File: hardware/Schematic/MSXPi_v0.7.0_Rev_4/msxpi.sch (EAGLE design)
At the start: 32 parts, among them IC1 LD117AS33TR

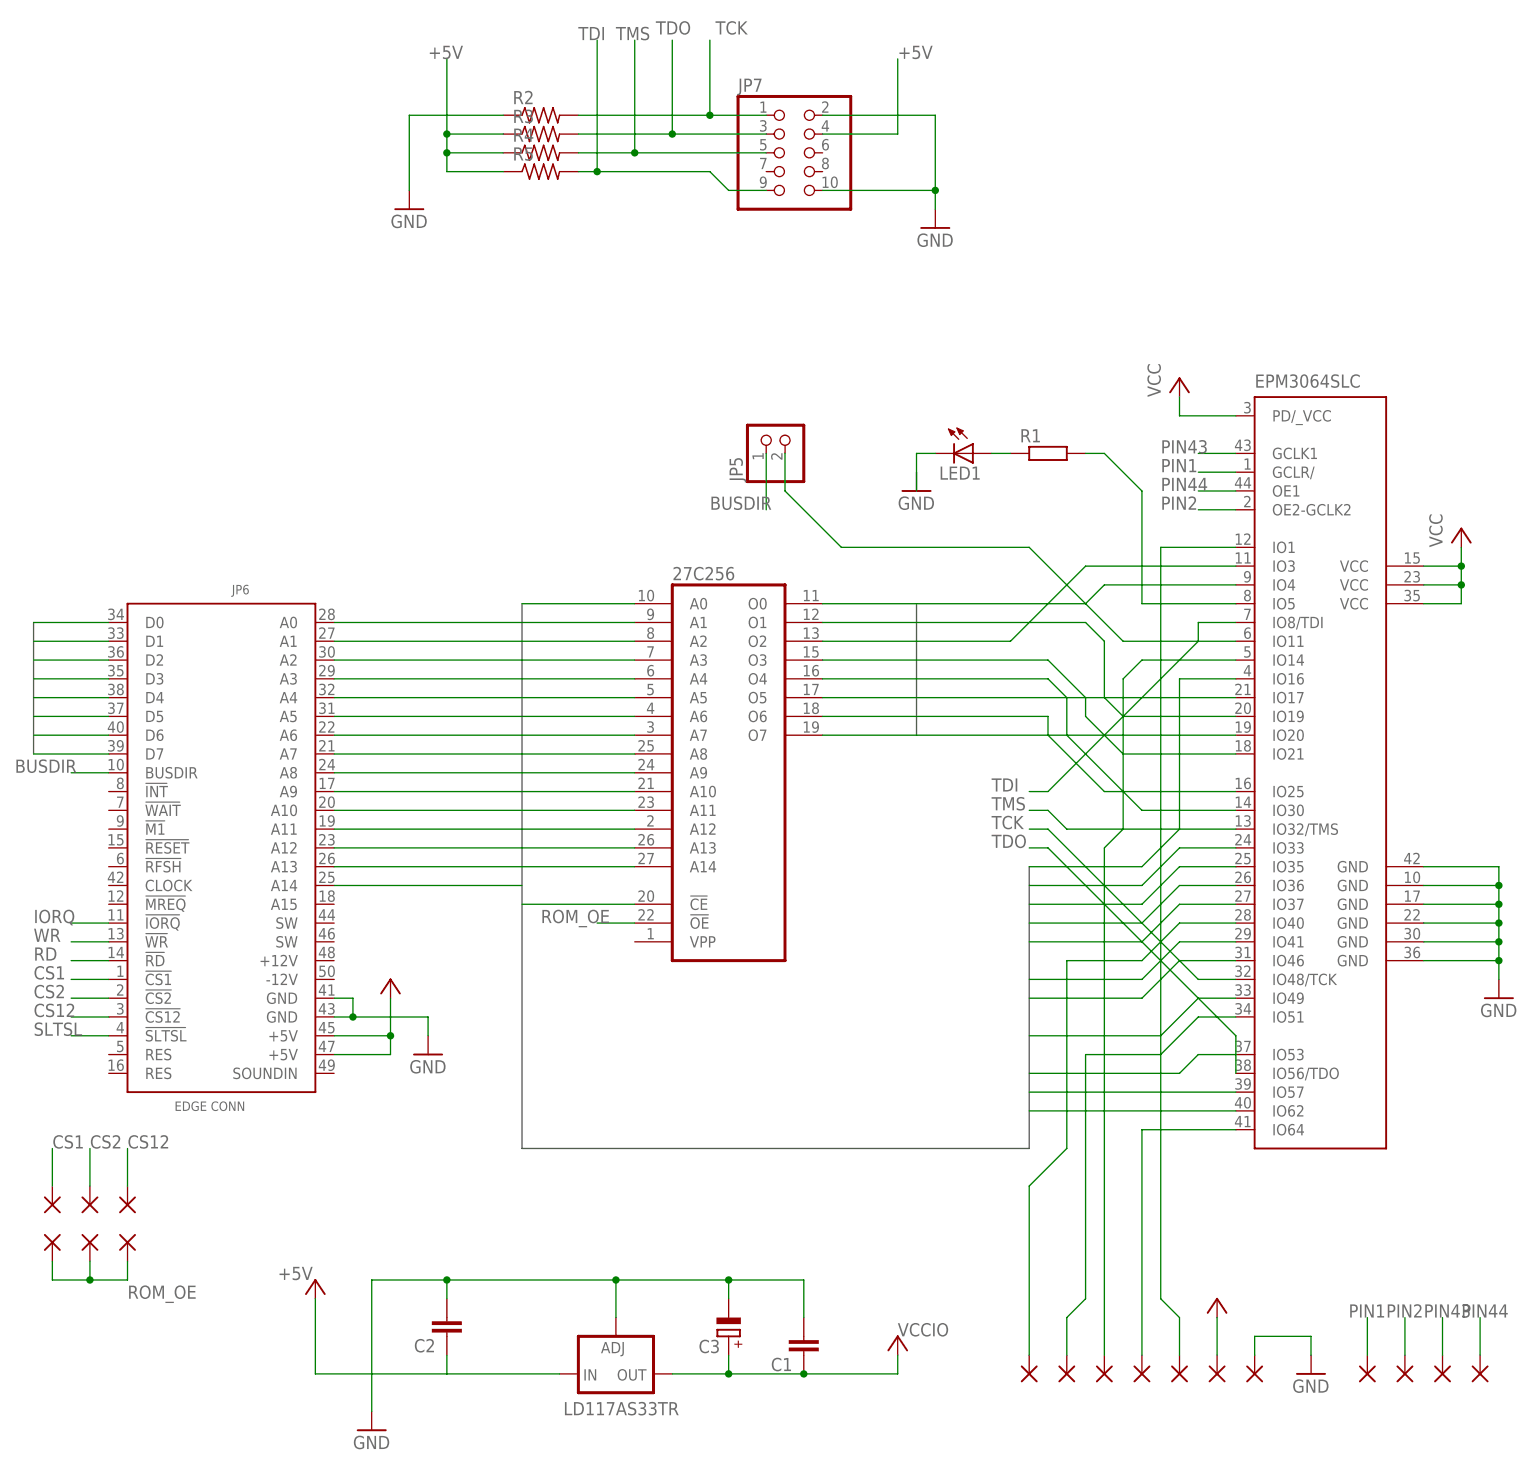
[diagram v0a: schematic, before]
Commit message: master branch now contain latest develoment branch, v20170705.00060. Contain MSXP-DOS, Tools, NFS, disk images
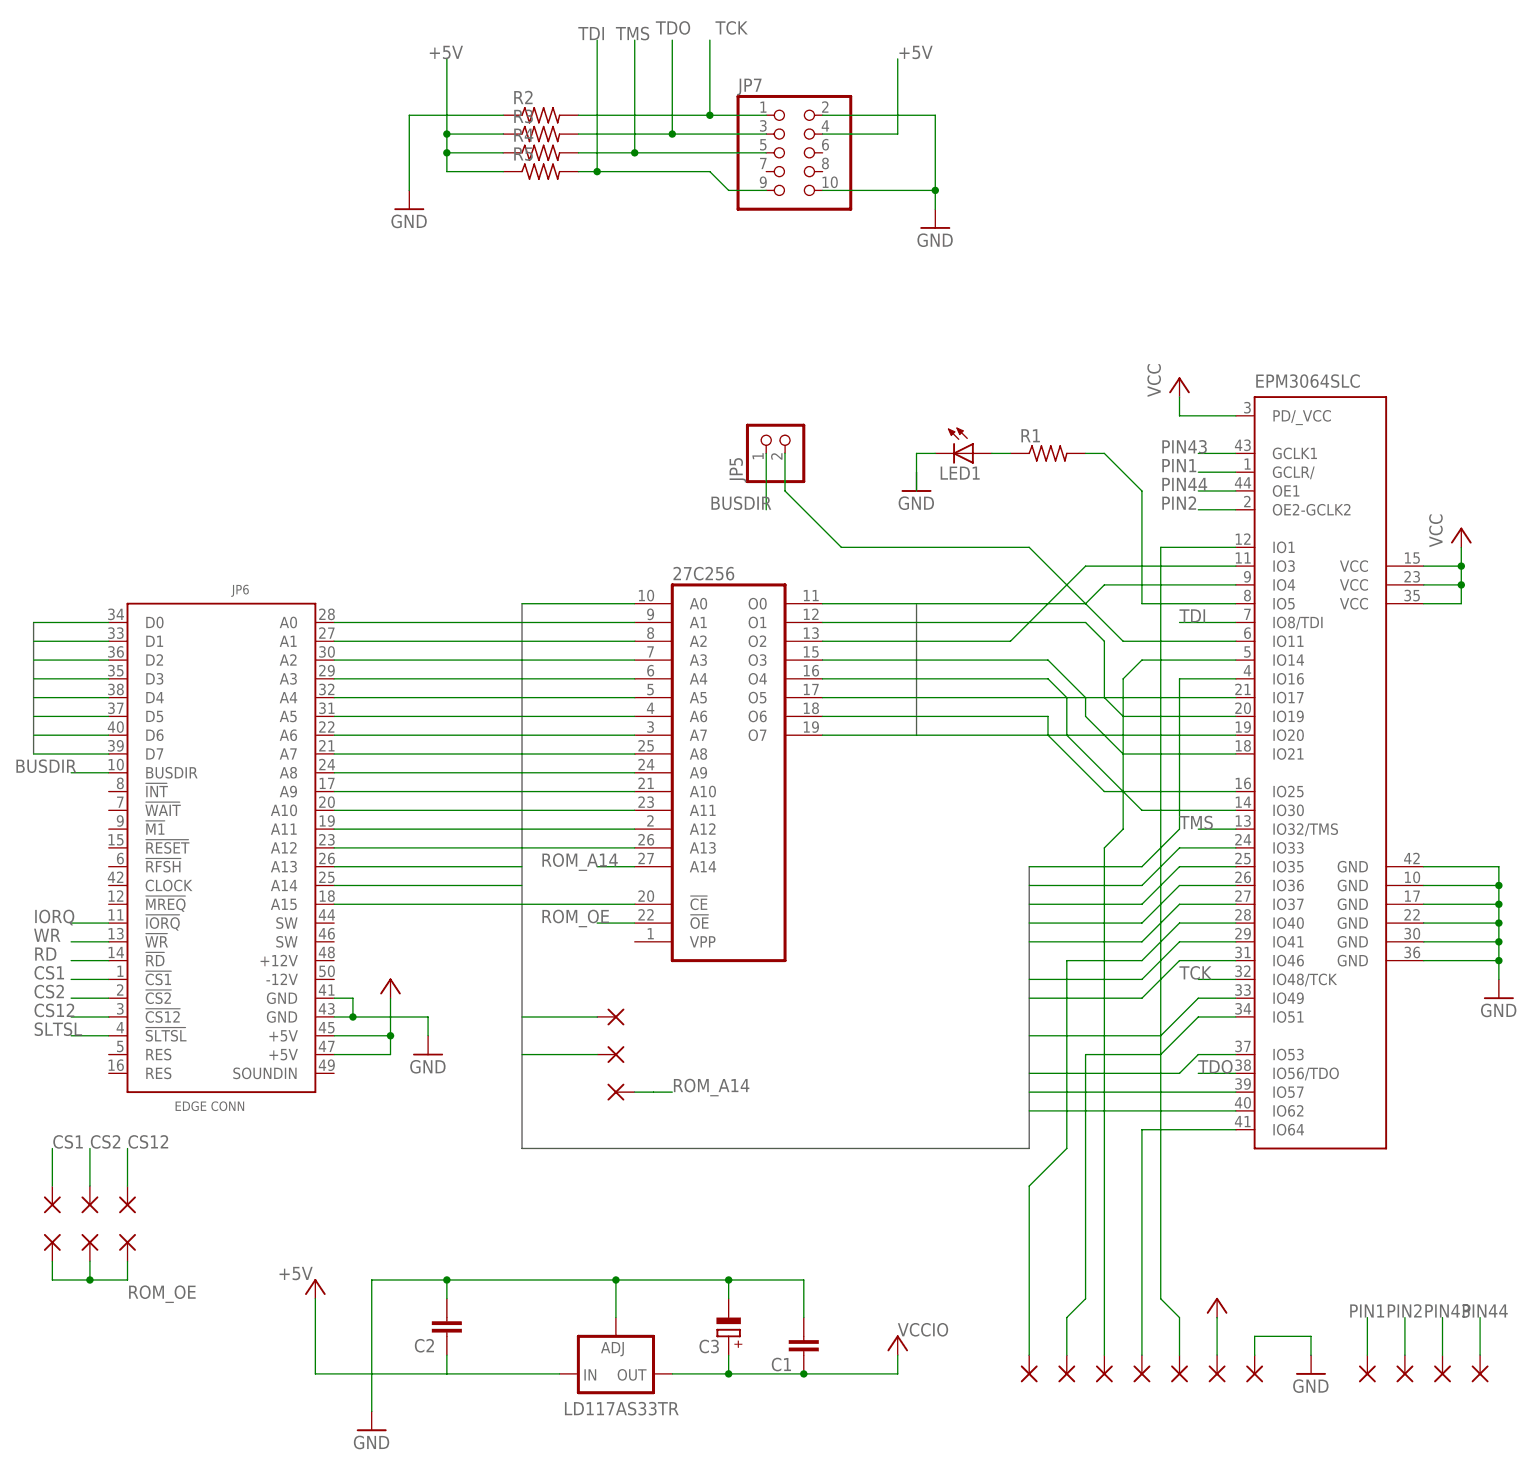
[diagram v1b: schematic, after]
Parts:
- added A14, A15, ROM_OE: (no value), wirepad:2,15/1,0
- R1: device rcl:R-EU_0207/7 -> rcl:R-US_0207/7
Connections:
- new net A15: A15.P, JP6.A15
- new net ROM_A14: 27C256A.A14, ROM_OE.P
- net A14: now also A14.P; no longer 27C256A.A14
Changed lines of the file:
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@@
 </layers>
 <schematic xreflabel="%F%N/%S.%C%R" xrefpart="/%S.%C%R">
+<description>Rev.3
+- Added GPIO access to CPLD Pins 1,2,43,44
+- Added DIP Switch to Select ROM_OE signal from:CS1 / CS2 / CS12
+Rev.4
+- Added DIP Switch to link MSX_A14/A15-&gt;ROM_A14</description>
 <attributes>
 </attributes>
@@
 <part name="P+2" library="supply1" deviceset="VCC" device=""/>
 <part name="EPM3064SLC" library="EPM3064-PLCC" deviceset="EPM3064" device="S44"/>
-<part name="R1" library="rcl" deviceset="R-EU_" device="0207/7"/>
 <part name="GND3" library="supply1" deviceset="GND" device=""/>
 <part name="P+4" library="supply1" deviceset="VCC" device=""/>
@@
 <part name="GND11" library="wirepad" deviceset="2,15/1,0" device=""/>
 <part name="C3" library="rcl" deviceset="CPOL-EU" device="E2.5-5"/>
+<part name="A15" library="wirepad" deviceset="2,15/1,0" device=""/>
+<part name="ROM_OE" library="wirepad" deviceset="2,15/1,0" device=""/>
+<part name="A14" library="wirepad" deviceset="2,15/1,0" device=""/>
+<part name="R1" library="rcl" deviceset="R-US_" device="0207/7"/>
 </parts>
 <sheets>
@@
 <attribute name="NAME" x="154.94" y="57.15" size="1.778" layer="95"/>
 </instance>
-<instance part="R1" gate="G$1" x="127" y="48.26"/>
 <instance part="GND3" gate="1" x="187.96" y="-25.4"/>
 <instance part="P+4" gate="VCC" x="182.88" y="38.1"/>
@@
 </instance>
 <instance part="C3" gate="G$1" x="83.82" y="-71.12" rot="R180"/>
+<instance part="A15" gate="1" x="68.58" y="-33.02" smashed="yes" rot="R180">
+<attribute name="VALUE" x="69.723" y="-29.718" size="1.778" layer="96" rot="R180"/>
+</instance>
+<instance part="ROM_OE" gate="1" x="68.58" y="-38.1" smashed="yes">
+<attribute name="VALUE" x="67.437" y="-41.402" size="1.778" layer="96"/>
+</instance>
+<instance part="A14" gate="1" x="68.58" y="-27.94" smashed="yes" rot="R180">
+<attribute name="VALUE" x="69.723" y="-24.638" size="1.778" layer="96" rot="R180"/>
+</instance>
+<instance part="R1" gate="G$1" x="127" y="48.26"/>
 </instances>
 <busses>
-<bus name="A[0..14],CS1,SLTSL,RD,WR,IORQ">
+<bus name="A[0..15],CS1,SLTSL,RD,WR,IORQ">
 <segment>
 <wire x1="124.46" y1="-45.72" x2="124.46" y2="-7.62" width="0.762" layer="92"/>
@@
 <net name="A14" class="0">
 <segment>
-<pinref part="27C256" gate="A" pin="A14"/>
-<wire x1="71.12" y1="-7.62" x2="55.88" y2="-7.62" width="0.1524" layer="91"/>
-</segment>
-<segment>
 <pinref part="JP6" gate="CRTRDG" pin="A14"/>
 <wire x1="55.88" y1="-10.16" x2="30.48" y2="-10.16" width="0.1524" layer="91"/>
+</segment>
+<segment>
+<pinref part="A14" gate="1" pin="P"/>
+<wire x1="55.88" y1="-27.94" x2="66.04" y2="-27.94" width="0.1524" layer="91"/>
 </segment>
 </net>
@@
 <pinref part="EPM3064SLC" gate="0" pin="IO48/TCK"/>
 <wire x1="152.4" y1="-22.86" x2="147.32" y2="-22.86" width="0.1524" layer="91"/>
-<wire x1="147.32" y1="-22.86" x2="127" y2="-2.54" width="0.1524" layer="91"/>
-<wire x1="127" y1="-2.54" x2="124.46" y2="-2.54" width="0.1524" layer="91"/>
-<label x="119.38" y="-2.54" size="1.778" layer="95"/>
+<label x="144.78" y="-22.86" size="1.778" layer="95"/>
 </segment>
 </net>
@@
 <segment>
 <pinref part="EPM3064SLC" gate="0" pin="IO56/TDO"/>
-<wire x1="152.4" y1="-35.56" x2="152.4" y2="-30.48" width="0.1524" layer="91"/>
-<wire x1="152.4" y1="-30.48" x2="127" y2="-5.08" width="0.1524" layer="91"/>
-<wire x1="127" y1="-5.08" x2="124.46" y2="-5.08" width="0.1524" layer="91"/>
-<label x="119.38" y="-5.08" size="1.778" layer="95"/>
+<wire x1="152.4" y1="-35.56" x2="147.32" y2="-35.56" width="0.1524" layer="91"/>
+<label x="147.32" y="-35.56" size="1.778" layer="95"/>
 </segment>
 </net>
@@
 <segment>
 <pinref part="EPM3064SLC" gate="0" pin="IO32/TMS"/>
-<wire x1="152.4" y1="-2.54" x2="129.54" y2="-2.54" width="0.1524" layer="91"/>
-<wire x1="129.54" y1="-2.54" x2="127" y2="0" width="0.1524" layer="91"/>
-<wire x1="127" y1="0" x2="124.46" y2="0" width="0.1524" layer="91"/>
-<label x="119.38" y="0" size="1.778" layer="95"/>
+<wire x1="152.4" y1="-2.54" x2="147.32" y2="-2.54" width="0.1524" layer="91"/>
+<label x="144.78" y="-2.54" size="1.778" layer="95"/>
 </segment>
 </net>
@@
 <segment>
 <pinref part="EPM3064SLC" gate="0" pin="IO8/TDI"/>
-<wire x1="152.4" y1="25.4" x2="147.32" y2="25.4" width="0.1524" layer="91"/>
-<wire x1="147.32" y1="25.4" x2="147.32" y2="22.86" width="0.1524" layer="91"/>
-<wire x1="147.32" y1="22.86" x2="127" y2="2.54" width="0.1524" layer="91"/>
-<wire x1="127" y1="2.54" x2="124.46" y2="2.54" width="0.1524" layer="91"/>
-<label x="119.38" y="2.54" size="1.778" layer="95"/>
+<wire x1="152.4" y1="25.4" x2="144.78" y2="25.4" width="0.1524" layer="91"/>
+<label x="144.78" y="25.4" size="1.778" layer="95"/>
 </segment>
 </net>
@@
 </segment>
 </net>
+<net name="A15" class="0">
+<segment>
+<pinref part="JP6" gate="CRTRDG" pin="A15"/>
+<wire x1="55.88" y1="-12.7" x2="30.48" y2="-12.7" width="0.1524" layer="91"/>
+</segment>
+<segment>
+<pinref part="A15" gate="1" pin="P"/>
+<wire x1="55.88" y1="-33.02" x2="66.04" y2="-33.02" width="0.1524" layer="91"/>
+</segment>
+</net>
+<net name="ROM_A14" class="0">
+<segment>
+<pinref part="27C256" gate="A" pin="A14"/>
+<wire x1="71.12" y1="-7.62" x2="66.04" y2="-7.62" width="0.1524" layer="91"/>
+<label x="58.42" y="-7.62" size="1.778" layer="95"/>
+</segment>
+<segment>
+<pinref part="ROM_OE" gate="1" pin="P"/>
+<wire x1="71.12" y1="-38.1" x2="73.66" y2="-38.1" width="0.1524" layer="91"/>
+<wire x1="73.66" y1="-38.1" x2="76.2" y2="-38.1" width="0.1524" layer="91"/>
+<label x="76.2" y="-38.1" size="1.778" layer="95"/>
+</segment>
+</net>
